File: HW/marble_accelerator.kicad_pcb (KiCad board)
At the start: 2 copper layers, 60 x 60 mm, 23 parts, among them J2 Conn_01x02_Pin, J3 Conn_01x02_Pin, J4 Conn_01x03_Pin, J5 Conn_01x03_Pin, J6 Conn_01x02_Pin, Q1 AO4892, U1 ATmega88P-20A, U2 CNY70, U3 ACS712xLCTR-05B, U4 ACS712xLCTR-05B, U5 L78L05_SO8, U6 EL7202CS

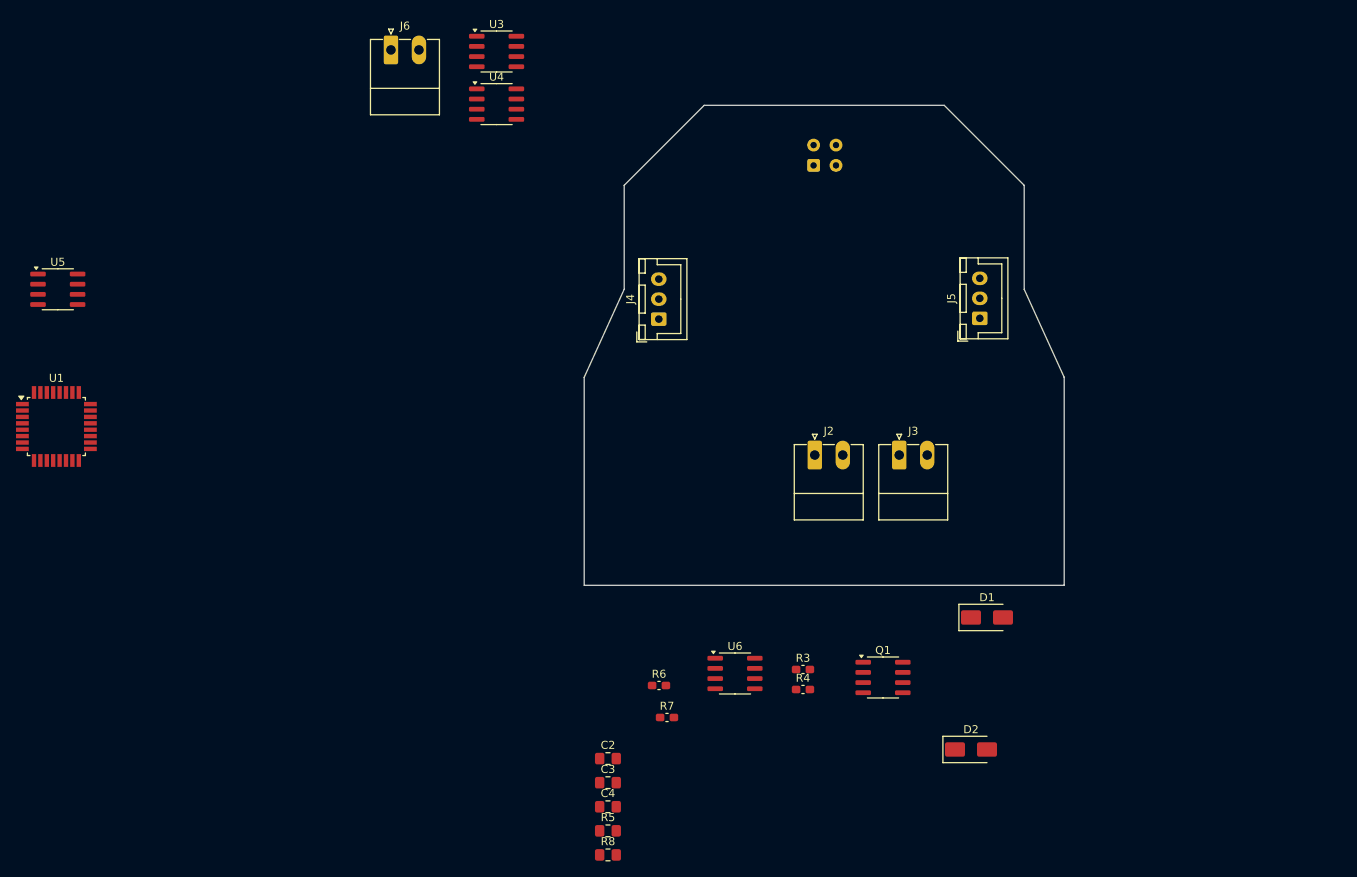
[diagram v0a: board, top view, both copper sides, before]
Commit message: update HW, reduce board to 5x5 cm
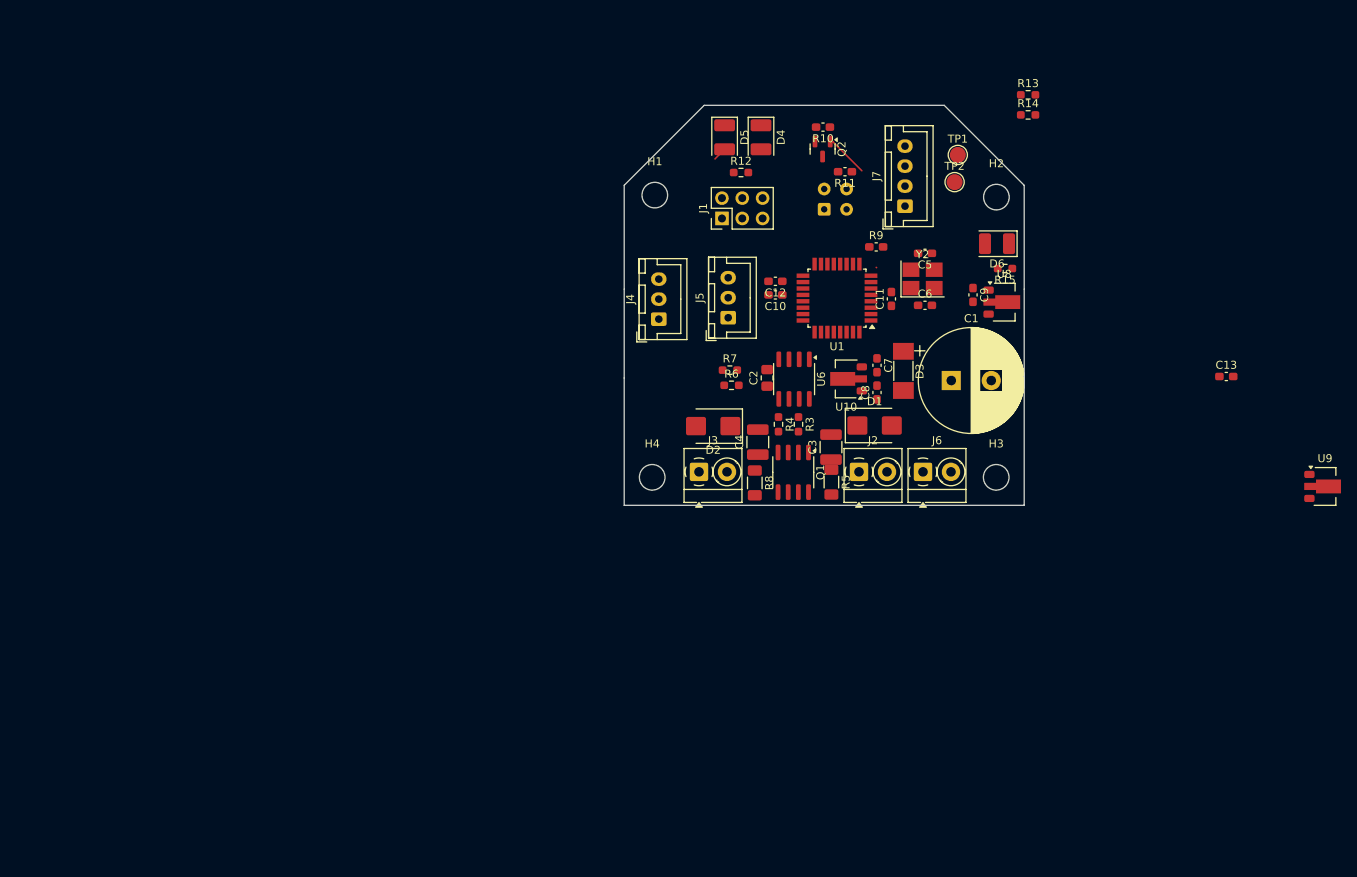
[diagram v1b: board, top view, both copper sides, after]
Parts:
- removed U3, U4: ACS712xLCTR-05B, Package_SO:SOIC-8_3.9x4.9mm_P1.27mm
- removed U5: L78L05_SO8, Package_SO:SOIC-8_3.9x4.9mm_P1.27mm
- added C1: 470µF/50V, Capacitor_THT:CP_Radial_D13.0mm_P5.00mm, F.Cu at (140.9, 74.4)
- added C10: 100nF, Capacitor_SMD:C_0603_1608Metric_Pad1.08x0.95mm_HandSolder, F.Cu at (118.9, 63.7)
- added C11: 100nF, Capacitor_SMD:C_0603_1608Metric_Pad1.08x0.95mm_HandSolder, F.Cu at (133.4, 64.2)
- added C12: 100nF, Capacitor_SMD:C_0603_1608Metric_Pad1.08x0.95mm_HandSolder, F.Cu at (118.9, 62.0)
- added C13: 100nF, Capacitor_SMD:C_0603_1608Metric_Pad1.08x0.95mm_HandSolder, F.Cu at (175.3, 73.9)
- added C5: 22pF, Capacitor_SMD:C_0603_1608Metric_Pad1.08x0.95mm_HandSolder, F.Cu at (137.6, 58.5)
- added C6: 22pF, Capacitor_SMD:C_0603_1608Metric_Pad1.08x0.95mm_HandSolder, F.Cu at (137.6, 65.0)
- added C7: 100nF, Capacitor_SMD:C_0603_1608Metric_Pad1.08x0.95mm_HandSolder, F.Cu at (131.6, 72.5)
- added C8: 100nF, Capacitor_SMD:C_0603_1608Metric_Pad1.08x0.95mm_HandSolder, F.Cu at (131.6, 75.9)
- added C9: 100nF, Capacitor_SMD:C_0603_1608Metric_Pad1.08x0.95mm_HandSolder, F.Cu at (143.6, 63.7)
- added D3: 1N4007, Resistor_SMD:R_MELF_MMB-0207, F.Cu at (134.9, 73.2)
- added D4: LED, LED_SMD:LED_PLCC-2_3.4x3.0mm_KA, F.Cu at (117.1, 44.0)
- added D5: LED, LED_SMD:LED_PLCC-2_3.4x3.0mm_KA, F.Cu at (112.5, 44.0)
- added D6: LED, LED_SMD:LED_PLCC-2_3.4x3.0mm_KA, F.Cu at (146.6, 57.3)
- added H1: MountingHole, MountingHole:MountingHole_3.2mm_M3, F.Cu at (103.8, 51.2)
- added H2: MountingHole, MountingHole:MountingHole_3.2mm_M3, F.Cu at (146.5, 51.5)
- added H3: MountingHole, MountingHole:MountingHole_3.2mm_M3, F.Cu at (146.5, 86.5)
- added H4: MountingHole, MountingHole:MountingHole_3.2mm_M3, F.Cu at (103.5, 86.5)
- added J1: AVR-ISP-6, Connector_PinHeader_2.54mm:PinHeader_2x03_P2.54mm_Vertical, F.Cu at (112.2, 54.1)
- added J7: Conn_01x04_Pin, Connector_JST:JST_XH_B4B-XH-A_1x04_P2.50mm_Vertical, F.Cu at (135.1, 52.6)
- added Q2: BSS138, Package_TO_SOT_SMD:SOT-23, F.Cu at (124.8, 45.5)
- added R10: 10k, Capacitor_SMD:C_0603_1608Metric_Pad1.08x0.95mm_HandSolder, F.Cu at (124.8, 42.7)
- added R11: 150R, Capacitor_SMD:C_0603_1608Metric_Pad1.08x0.95mm_HandSolder, F.Cu at (127.6, 48.3)
- added R12: 10k, Resistor_SMD:R_0603_1608Metric_Pad0.98x0.95mm_HandSolder, F.Cu at (114.6, 48.4)
- added R13: 10k, Resistor_SMD:R_0603_1608Metric_Pad0.98x0.95mm_HandSolder, F.Cu at (150.5, 38.7)
- added R14: 10k, Resistor_SMD:R_0603_1608Metric_Pad0.98x0.95mm_HandSolder, F.Cu at (150.5, 41.2)
- added R15: 10k, Resistor_SMD:R_0603_1608Metric_Pad0.98x0.95mm_HandSolder, F.Cu at (147.6, 60.4)
- added R9: 10k, Capacitor_SMD:C_0603_1608Metric_Pad1.08x0.95mm_HandSolder, F.Cu at (131.5, 57.7)
- added TP1: TestPoint, TestPoint:TestPoint_Pad_D2.0mm, F.Cu at (141.7, 46.2)
- added TP2: TestPoint, TestPoint:TestPoint_Pad_D2.0mm, F.Cu at (141.3, 49.6)
- added U10: L78L12_SOT89, Package_TO_SOT_SMD:SOT-89-3, F.Cu at (127.8, 74.2)
- added U8: L78L05_SOT89, Package_TO_SOT_SMD:SOT-89-3, F.Cu at (147.5, 64.6)
- added U9: MCP1703Ax-500xxMB, Package_TO_SOT_SMD:SOT-89-3, F.Cu at (187.6, 87.6)
- added Y2: Crystal_GND24_Small, Crystal:Crystal_SMD_3225-4Pin_3.2x2.5mm_HandSoldering, F.Cu at (137.3, 61.7)
- C3, C4: footprint Capacitor_SMD:C_0805_2012Metric_Pad1.18x1.45mm_HandSolder -> Capacitor_SMD:C_1210_3225Metric_Pad1.33x2.70mm_HandSolder
- D1, D2: value SMAJ24CA -> SMBJ24CA; footprint Diode_SMD:D_SMA -> Diode_SMD:D_SMB
- J2, J3, J6: footprint Connector_Phoenix_MC:PhoenixContact_MC_1,5_2-G-3.5_1x02_P3.50mm_Horizontal -> TerminalBlock_MetzConnect:TerminalBlock_MetzConnect_Type059_RT06302HBWC_1x02_P3.50mm_Horizontal
- Q1: value AO4892 -> DMTH6016LSD-13
- R3, R4, R6, R7: footprint Capacitor_SMD:C_0603_1608Metric_Pad1.08x0.95mm_HandSolder -> Resistor_SMD:R_0603_1608Metric_Pad0.98x0.95mm_HandSolder
- R5: footprint Capacitor_SMD:C_0805_2012Metric_Pad1.18x1.45mm_HandSolder -> Resistor_SMD:R_1206_3216Metric_Pad1.30x1.75mm_HandSolder
- R8: value 27 -> 47; footprint Capacitor_SMD:C_0805_2012Metric_Pad1.18x1.45mm_HandSolder -> Resistor_SMD:R_1206_3216Metric_Pad1.30x1.75mm_HandSolder
- moved U1 98.9 mm to (126.6, 64.1), turned to 180 degrees
- moved J6 84.9 mm to (137.3, 85.8)
- moved R5 51.8 mm to (125.9, 87.1), turned to -90 degrees
- moved D2 51.7 mm to (111.1, 80.1), turned to 180 degrees
- moved C2 51.6 mm to (117.9, 74.1), turned to 90 degrees
- moved C3 50.4 mm to (125.8, 82.7), turned to 90 degrees
- moved R8 50.0 mm to (116.3, 87.2), turned to -90 degrees
- moved C4 49.3 mm to (116.7, 82.1), turned to 90 degrees
- moved R7 44.1 mm to (113.2, 73.1)
- moved R6 38.6 mm to (113.4, 75.0)
- moved U6 37.5 mm to (121.2, 74.2), turned to -90 degrees
- moved R4 33.3 mm to (119.3, 79.9), turned to -90 degrees
- moved J5 31.5 mm to (113.0, 66.5)
- moved R3 30.7 mm to (121.8, 79.9), turned to -90 degrees
- moved Q1 28.0 mm to (121.1, 85.9), turned to -90 degrees
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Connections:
- J2 pad 1: unconnected-(J2-Pin_1-Pad1) -> /coil driver/COIL0_NEG
- J2 pad 2: unconnected-(J2-Pin_2-Pad2) -> Vdrive
- J3 pad 1: unconnected-(J3-Pin_1-Pad1) -> Vdrive
- J3 pad 2: unconnected-(J3-Pin_2-Pad2) -> /coil driver/COIL1_NEG
- J4 pad 1: unconnected-(J4-Pin_1-Pad1) -> /microcontroller/Hall1
- J4 pad 2: unconnected-(J4-Pin_2-Pad2) -> +5V
- J4 pad 3: unconnected-(J4-Pin_3-Pad3) -> GND
- J5 pad 1: unconnected-(J5-Pin_1-Pad1) -> /microcontroller/Hall0
- J5 pad 2: unconnected-(J5-Pin_2-Pad2) -> +5V
- J5 pad 3: unconnected-(J5-Pin_3-Pad3) -> GND
- J6 pad 1: unconnected-(J6-Pin_1-Pad1) -> Vdrive
- J6 pad 2: unconnected-(J6-Pin_2-Pad2) -> GND
- R6 pad 1: /coil driver/IN_FIRST_COIL -> /coil driver/IN_COIL0
- R7 pad 1: /coil driver/IN_SECOND_COIL -> /coil driver/IN_COIL1
- U1 pad 1: unconnected-(U1-PD3-Pad1) -> Net-(U1-PD3)
- U1 pad 10: unconnected-(U1-PD6-Pad10) -> Net-(D5-A)
- U1 pad 13: unconnected-(U1-PB1-Pad13) -> /microcontroller/EntryEnable
- U1 pad 15: unconnected-(U1-PB3-Pad15) -> /microcontroller/MOSI
- U1 pad 16: unconnected-(U1-PB4-Pad16) -> /microcontroller/MISO
- U1 pad 17: unconnected-(U1-PB5-Pad17) -> /microcontroller/SCK
- U1 pad 18: unconnected-(U1-AVCC-Pad18) -> +5V
- U1 pad 19: unconnected-(U1-ADC6-Pad19) -> /microcontroller/EntrySensor
- U1 pad 2: unconnected-(U1-PD4-Pad2) -> Net-(U1-PD4)
- U1 pad 20: unconnected-(U1-AREF-Pad20) -> Net-(U1-AREF)
- U1 pad 21: Net-(U1-GND-Pad21) -> GND
- U1 pad 23: unconnected-(U1-PC0-Pad23) -> /microcontroller/Hall0
- U1 pad 24: unconnected-(U1-PC1-Pad24) -> /microcontroller/Hall1
- U1 pad 25: unconnected-(U1-PC2-Pad25) -> /coil driver/IN_COIL1
- U1 pad 26: unconnected-(U1-PC3-Pad26) -> /coil driver/IN_COIL0
- U1 pad 29: unconnected-(U1-~{RESET}/PC6-Pad29) -> /microcontroller/!RST
- U1 pad 3: Net-(U1-GND-Pad21) -> GND
- U1 pad 30: unconnected-(U1-PD0-Pad30) -> Net-(J7-Pin_2)
- U1 pad 31: unconnected-(U1-PD1-Pad31) -> Net-(J7-Pin_3)
- U1 pad 4: Net-(U1-VCC-Pad4) -> +5V
- U1 pad 5: Net-(U1-GND-Pad21) -> GND
- U1 pad 6: Net-(U1-VCC-Pad4) -> +5V
- U1 pad 7: unconnected-(U1-XTAL1/PB6-Pad7) -> Net-(U1-XTAL1/PB6)
- U1 pad 8: unconnected-(U1-XTAL2/PB7-Pad8) -> Net-(U1-XTAL2/PB7)
- U1 pad 9: unconnected-(U1-PD5-Pad9) -> Net-(D4-A)
- U2 pad 1: unconnected-(U2-A-Pad1) -> Net-(U2-A)
- U2 pad 2: unconnected-(U2-K-Pad2) -> Net-(Q2-D)
- U2 pad 3: unconnected-(U2-C-Pad3) -> +5V
- U2 pad 4: unconnected-(U2-E-Pad4) -> /microcontroller/EntrySensor
- U6 pad 2: /coil driver/IN_FIRST_COIL -> /coil driver/IN_COIL0
- U6 pad 4: /coil driver/IN_SECOND_COIL -> /coil driver/IN_COIL1
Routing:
- net /microcontroller/EntryEnable: track 0.00 -> 5.47 mm
- net Net-(D5-A): track 0.00 -> 1.77 mm
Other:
- board size 60 x 60 mm -> 50 x 50 mm

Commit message: update HW
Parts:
- added L1: 10µH, Inductor_SMD:L_0603_1608Metric_Pad1.05x0.95mm_HandSolder, F.Cu at (118.9, 60.3)
- added R16: 30k, Resistor_SMD:R_0603_1608Metric_Pad0.98x0.95mm_HandSolder, F.Cu at (104.7, 73.9)
- added R17: 10k, Resistor_SMD:R_0603_1608Metric_Pad0.98x0.95mm_HandSolder, F.Cu at (104.7, 72.1)
- added TP3: TestPoint, TestPoint:TestPoint_Pad_D2.0mm, F.Cu at (137.4, 68.0)
- moved R14 42.3 mm to (108.5, 46.0), turned to 90 degrees
- moved C13 32.7 mm to (143.6, 65.7), turned to 90 degrees
- moved R13 31.3 mm to (120.3, 46.9), turned to 90 degrees
- moved R6 8.93 mm to (119.2, 68.2), turned to 180 degrees
- moved R7 6.84 mm to (119.2, 69.8), turned to 180 degrees
- moved R11 6.64 mm to (121.9, 51.7), turned to -90 degrees
- moved D5 4.45 mm to (117.0, 43.9), turned to 90 degrees
- moved D4 4.10 mm to (113.0, 43.8), turned to 90 degrees
- moved C9 1.30 mm to (143.6, 62.4)
- moved U8 0.80 mm to (147.5, 63.8)
- moved R15 0.70 mm to (147.6, 59.7)
- moved C3 0.63 mm to (125.5, 82.2)
- moved R5 0.41 mm to (125.5, 87.2)
- moved R8 0.38 mm to (116.7, 87.2)
- moved H1 0.37 mm to (103.5, 51.4)
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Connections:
- C12 pad 1: +5V -> Net-(U1-AVCC)
- U1 pad 18: +5V -> Net-(U1-AVCC)
- U1 pad 22: unconnected-(U1-ADC7-Pad22) -> Net-(U1-ADC7)
- U1 pad 27: unconnected-(U1-PC4-Pad27) -> Net-(U1-PC4)
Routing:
- net Vdrive: track 0.00 -> 54.7 mm
- net Net-(J7-Pin_3): track 0.00 -> 38.0 mm
- net Net-(D4-A): track 0.00 -> 36.8 mm
- net Net-(J7-Pin_2): track 0.00 -> 35.9 mm
- net Net-(D5-A): track 1.77 -> 31.9 mm
- net Net-(U1-ADC7): track 0.00 -> 27.6 mm
- net /microcontroller/Hall1: track 0.00 -> 18.8 mm
- net /microcontroller/EntryEnable: track 5.47 -> 22.8 mm
- net /coil driver/COIL1_NEG: track 0.00 -> 15.1 mm
- net /microcontroller/MISO: track 0.00 -> 14.9 mm
- net /coil driver/COIL0_NEG: track 0.00 -> 14.8 mm
- net Net-(U1-PC4): track 0.00 -> 14.7 mm
- net +12V: track 0.00 -> 14.6 mm
- net GND: track 0.00 -> 13.9 mm
- net Net-(D3-K): track 0.00 -> 13.8 mm
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
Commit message: update layout
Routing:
- net /microcontroller/SCK: track 0.00 -> 28.1 mm
- net Net-(D4-K): track 0.00 -> 4.59 mm
- net +5V: track 8.98 -> 13.1 mm
- net /microcontroller/MOSI: track 13.4 -> 17.3 mm
- net Net-(D5-K): track 0.00 -> 3.54 mm
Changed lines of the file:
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@@
+	)
+	(segment
+		(start 113.6875 48.4)
+		(end 113.1 48.4)
+		(width 0.2)
+		(layer "F.Cu")
+		(net 18)
+	)
+	(segment
+		(start 112.22 49.28)
+		(end 112.22 51.6)
+		(width 0.2)
+		(layer "F.Cu")
+		(net 18)
+	)
+	(segment
+		(start 113.1 48.4)
+		(end 112.22 49.28)
+		(width 0.2)
+		(layer "F.Cu")
+		(net 18)
 	)
 	(segment
@@
 	)
 	(segment
+		(start 112.5 52.989)
+		(end 112.5 52.94776)
+		(width 0.2)
+		(layer "F.Cu")
+		(net 23)
+	)
+	(segment
+		(start 121.3 61.3)
+		(end 121 61)
+		(width 0.2)
+		(layer "F.Cu")
+		(net 23)
+	)
+	(segment
+		(start 115.449 50.449)
+		(end 115.911 50.911)
+		(width 0.2)
+		(layer "F.Cu")
+		(net 23)
+	)
+	(segment
+		(start 114.051 50.449)
+		(end 115.449 50.449)
+		(width 0.2)
+		(layer "F.Cu")
+		(net 23)
+	)
+	(segment
+		(start 110.5 54.722)
+		(end 110.5 53.5)
+		(width 0.2)
+		(layer "F.Cu")
+		(net 23)
+	)
+	(segment
+		(start 121 59)
+		(end 119.5 57.5)
+		(width 0.2)
+		(layer "F.Cu")
+		(net 23)
+	)
+	(segment
+		(start 119.5 57.5)
+		(end 113.278 57.5)
+		(width 0.2)
+		(layer "F.Cu")
+		(net 23)
+	)
+	(segment
+		(start 121 61)
+		(end 121 59)
+		(width 0.2)
+		(layer "F.Cu")
+		(net 23)
+	)
+	(segment
+		(start 112.5 52.94776)
+		(end 113.371 52.07676)
+		(width 0.2)
+		(layer "F.Cu")
+		(net 23)
+	)
+	(segment
+		(start 110.5 53.5)
+		(end 111.011 52.989)
+		(width 0.2)
+		(layer "F.Cu")
+		(net 23)
+	)
+	(segment
+		(start 115.911 52.989)
+		(end 114.76 54.14)
+		(width 0.2)
+		(layer "F.Cu")
+		(net 23)
+	)
+	(segment
+		(start 113.371 52.07676)
+		(end 113.371 51.129)
+		(width 0.2)
+		(layer "F.Cu")
+		(net 23)
+	)
+	(segment
+		(start 111.011 52.989)
+		(end 112.5 52.989)
+		(width 0.2)
+		(layer "F.Cu")
+		(net 23)
+	)
+	(segment
+		(start 122.35 61.3)
+		(end 121.3 61.3)
+		(width 0.2)
+		(layer "F.Cu")
+		(net 23)
+	)
+	(segment
+		(start 115.911 50.911)
+		(end 115.911 52.989)
+		(width 0.2)
+		(layer "F.Cu")
+		(net 23)
+	)
+	(segment
+		(start 113.278 57.5)
+		(end 110.5 54.722)
+		(width 0.2)
+		(layer "F.Cu")
+		(net 23)
+	)
+	(segment
+		(start 113.371 51.129)
+		(end 114.051 50.449)
+		(width 0.2)
+		(layer "F.Cu")
+		(net 23)
+	)
+	(segment
 		(start 115.199 56.599)
 		(end 113.609 55.009)
@@
 		(start 124.6 59.1)
 		(end 122.099 56.599)
+		(width 0.2)
+		(layer "F.Cu")
+		(net 25)
+	)
+	(segment
+		(start 113.609 52.751)
+		(end 113.609 55.009)
+		(width 0.2)
+		(layer "F.Cu")
+		(net 25)
+	)
+	(segment
+		(start 114.76 51.6)
+		(end 113.609 52.751)
 		(width 0.2)
 		(layer "F.Cu")
@@
 	)
 	(segment
+		(start 108.7125 45.3)
+		(end 108.5 45.0875)
+		(width 0.2)
+		(layer "F.Cu")
+		(net 38)
+	)
+	(segment
+		(start 113 45.3)
+		(end 108.7125 45.3)
+		(width 0.2)
+		(layer "F.Cu")
+		(net 38)
+	)
+	(segment
 		(start 130.6 42.7)
 		(end 128.5 40.6)
@@
 	)
 	(segment
+		(start 117 45.4)
+		(end 119.7125 45.4)
+		(width 0.2)
+		(layer "F.Cu")
+		(net 41)
+	)
+	(segment
+		(start 119.7125 45.4)
+		(end 120.3 45.9875)
+		(width 0.2)
+		(layer "F.Cu")
+		(net 41)
+	)
+	(segment

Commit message: update layout
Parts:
- added C14: 100nF, Capacitor_SMD:C_0603_1608Metric_Pad1.08x0.95mm_HandSolder, F.Cu at (104.6, 70.5)
- moved TP3 0.10 mm to (137.5, 68.0)
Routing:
- net /microcontroller/!RST: track 0.00 -> 36.3 mm, vias 0 -> 3
- net +12V: track 14.6 -> 42.1 mm
- net Vdrive: track 54.7 -> 63.7 mm
- net Net-(U1-ADC7): track 27.6 -> 31.0 mm
- net Net-(J7-Pin_2): track 35.9 -> 35.1 mm

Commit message: update layout and schematic
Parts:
- removed U9: MCP1703Ax-500xxMB, Package_TO_SOT_SMD:SOT-89-3
- added R18: 0R, Resistor_SMD:R_0603_1608Metric_Pad0.98x0.95mm_HandSolder, F.Cu at (132.1, 74.4)
- C14: value 100nF -> 100µF/25V; footprint Capacitor_SMD:C_0603_1608Metric_Pad1.08x0.95mm_HandSolder -> Capacitor_THT:CP_Radial_D6.3mm_P2.50mm
- moved R15 48.7 mm to (102.6, 78.3)
- moved D6 46.6 mm to (102.9, 73.3), turned to 90 degrees
- moved C14 38.8 mm to (141.0, 57.0)
- moved R9 11.3 mm to (128.0, 47.0), turned to 90 degrees
- moved R6 7.29 mm to (125.8, 71.3), turned to 0 degrees
- moved R17 4.66 mm to (109.2, 73.3), turned to 180 degrees
- moved R16 4.63 mm to (109.2, 75.0), turned to 0 degrees
- moved J5 2.07 mm to (111.0, 66.0)
- moved C11 1.20 mm to (132.2, 64.2)
- moved Y2 1.20 mm to (136.1, 61.7)
- moved C10 1.20 mm to (117.7, 63.7)
- moved C12 1.20 mm to (117.7, 62.0)
- moved L1 1.20 mm to (117.7, 60.3)
- moved C6 1.20 mm to (136.4, 65.0)
- moved U1 1.20 mm to (125.4, 64.1)
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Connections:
- C14 pad 1: Net-(U1-ADC7) -> +5V
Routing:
- net /microcontroller/!RST: track 36.3 -> 0.00 mm, vias 3 -> 0
- net +12V: track 42.1 -> 9.66 mm
- net Net-(U1-ADC7): track 31.0 -> 0.00 mm
- net /microcontroller/EntrySensor: track 0.00 -> 20.9 mm, vias 0 -> 4
- net +5V: track 13.1 -> 22.8 mm
- net /microcontroller/SCK: track 28.1 -> 20.1 mm
- net Net-(D4-K): track 4.59 -> 0.00 mm
- net /coil driver/COIL0_NEG: track 14.8 -> 19.1 mm
- net Net-(D3-K): track 13.8 -> 9.91 mm
- net GND: track 13.9 -> 10.3 mm, vias 0 -> 10
- net Net-(D5-K): track 3.54 -> 0.00 mm
- net /microcontroller/MOSI: track 17.5 -> 15.5 mm
- net /coil driver/IN_COIL0: track 9.31 -> 7.32 mm, vias 2 -> 0
- net Net-(J7-Pin_3): track 38.4 -> 36.6 mm
- net Net-(U1-AVCC): track 4.33 -> 2.65 mm
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- added copper zone on F.Cu, net /coil driver/COIL0_NEG
- added copper zone on F.Cu, net /coil driver/COIL1_NEG
- added copper zone on B.Cu, net GND
- added copper zone on F.Cu, net GND

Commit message: update schematic and board
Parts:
- moved TP3 14.5 mm to (147.8, 57.8)
- moved TP2 12.6 mm to (131.3, 57.2)
- moved R7 1.10 mm to (118.1, 69.7)
- moved D3 0.73 mm to (135.1, 73.9)
- moved R15 0.28 mm to (102.8, 78.1), turned to 0 degrees
- moved R4 0.08 mm to (119.2, 79.9)
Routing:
- net /microcontroller/!RST: track 0.00 -> 41.8 mm, vias 0 -> 5
- net Net-(U1-PD3): track 0.00 -> 40.9 mm
- net Net-(U1-ADC7): track 0.00 -> 36.9 mm
- net Net-(U1-PD4): track 0.00 -> 25.7 mm
- net Net-(U1-PC4): track 15.6 -> 37.6 mm
- net Net-(D3-K): track 9.91 -> 0.00 mm
- net +12V: track 9.66 -> 17.1 mm
- net Vdrive: track 64.7 -> 69.9 mm
- net +5V: track 22.8 -> 27.9 mm
- net Net-(J7-Pin_2): track 34.3 -> 38.2 mm
- net /coil driver/IN_COIL0: track 7.32 -> 4.44 mm
- net Net-(J7-Pin_3): track 36.6 -> 38.3 mm
- net /coil driver/IN_COIL1: track 5.68 -> 7.00 mm
- net GND: track 10.3 -> 10.8 mm, vias 10 -> 14

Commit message: finished first layout
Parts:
- added C6: 100nF, Capacitor_SMD:C_0603_1608Metric_Pad1.08x0.95mm_HandSolder, F.Cu at (109.2, 71.5)
- added R4: 1k, Capacitor_SMD:C_0603_1608Metric_Pad1.08x0.95mm_HandSolder, F.Cu at (117.7, 65.4)
- added R5: 1k, Capacitor_SMD:C_0603_1608Metric_Pad1.08x0.95mm_HandSolder, F.Cu at (117.7, 66.9)
- moved TP1 38.3 mm to (113.1, 74.0)
- moved R2 11.0 mm to (120.2, 54.7)
- moved R10 9.90 mm to (109.7, 57.0)
- moved R17 7.23 mm to (124.9, 75.1), turned to 90 degrees
- moved C14 6.16 mm to (126.4, 77.0), turned to 90 degrees
- moved C13 4.70 mm to (126.4, 73.7), turned to -90 degrees
- moved U4 3.01 mm to (130.0, 74.8), turned to 0 degrees
- moved C4 1.84 mm to (135.5, 56.9), turned to 0 degrees
- moved D6 1.60 mm to (102.9, 74.9)
- moved Y1 1.26 mm to (135.7, 60.5), turned to 90 degrees
- moved C5 0.89 mm to (136.0, 64.2), turned to 180 degrees
- moved D1 0.70 mm to (113.0, 44.5)
- moved D2 0.63 mm to (116.8, 44.5)
- moved R8 0.54 mm to (120.1, 46.4)
- moved TP2 0.45 mm to (141.3, 46.4)
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- renumbered C11 to C1, C9 to C10, C14 to C11, C13 to C12, C8 to C13, C7 to C14, C1 to C15, C12 to C2, C10 to C3, C5 to C4, C6 to C5, C2 to C7, C3 to C8, C4 to C9, D4 to D1, D5 to D2, D1 to D3, D2 to D4, D3 to D5, H2 to H1, H1 to H2, H4 to H3, H3 to H4, J6 to J1, J5 to J3, J3 to J4, J4 to J5, J7 to J6, J1 to J7, Q2 to Q1, Q1 to Q2, R11 to R1, R12 to R10, R5 to R11, R3 to R12, R6 to R13, R7 to R14, R4 to R15, R8 to R16, R18 to R17, R15 to R18, R9 to R2, R10 to R3, R16 to R6, R17 to R7, R13 to R8, R14 to R9, TP3 to TP1, TP1 to TP2, TP2 to TP3, U2 to U1, U1 to U2, U6 to U3, U10 to U4, U8 to U5, Y2 to Y1
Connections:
- D1 pad 2: Net-(D4-A) -> Net-(D1-A)
- D2 pad 2: Net-(D5-A) -> Net-(D2-A)
- J3 pad 1: /microcontroller/Hall0 -> Net-(J3-Pin_1)
- J5 pad 1: /microcontroller/Hall1 -> Net-(J5-Pin_1)
- R6 pad 2: Net-(U1-ADC7) -> Net-(U2-ADC6)
- R7 pad 1: Net-(U1-ADC7) -> Net-(U2-ADC6)
- U2 pad 10: Net-(D5-A) -> Net-(D1-A)
- U2 pad 11: unconnected-(U1-PD7-Pad11) -> Net-(D2-A)
- U2 pad 13: /microcontroller/EntryEnable -> unconnected-(U2-PB1-Pad13)
- U2 pad 19: /microcontroller/EntrySensor -> Net-(U2-ADC6)
- U2 pad 22: Net-(U1-ADC7) -> /microcontroller/Hall0
- U2 pad 23: /microcontroller/Hall0 -> /microcontroller/Hall1
- U2 pad 24: /microcontroller/Hall1 -> /microcontroller/EntrySensor
- U2 pad 9: Net-(D4-A) -> /microcontroller/EntryEnable
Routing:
- net +5V: track 27.9 -> 120.8 mm, vias 0 -> 4
- net Net-(D4-A): track 37.3 -> 0.00 mm
- net Net-(U1-ADC7): track 36.9 -> 0.00 mm
- net GND: track 10.8 -> 47.7 mm, vias 14 -> 70
- net Net-(D1-A): track 0.00 -> 36.9 mm, vias 0 -> 2
- net Net-(U2-ADC6): track 0.00 -> 35.9 mm
- net Net-(D5-A): track 32.4 -> 0.00 mm
- net Net-(D2-A): track 0.00 -> 27.5 mm
- net Net-(D5-K): track 0.00 -> 27.1 mm
- net Net-(U2-PC4): track 37.6 -> 17.1 mm, vias 0 -> 2
- net +12V: track 17.1 -> 37.5 mm
- net /microcontroller/Hall1: track 17.1 -> 3.09 mm
- net Net-(J5-Pin_1): track 0.00 -> 12.8 mm
- net /coil driver/COIL0_NEG: track 19.1 -> 6.79 mm
- net /microcontroller/EntrySensor: track 20.9 -> 32.7 mm
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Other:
- board text added: "+"
- board text added: "-"
- board text added: "1"
- board text added: "5V"
- board text added: "COIL1"
- board text added: "GND"
- board text added: "HALL0"
- board text added: "HALL1"
- board text added: "PWR"
- board text added: "RX"
- board text added: "TX"

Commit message: first HW order state
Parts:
- J6: value Conn_01x04_Pin -> UART; footprint Connector_JST:JST_XH_B4B-XH-A_1x04_P2.50mm_Vertical -> Connector_PinHeader_2.54mm:PinHeader_1x04_P2.54mm_Vertical
- moved Q1 0.15 mm to (125.0, 45.5)
- moved R3 0.15 mm to (125.0, 42.7)
- moved J6 0.14 mm to (135.0, 52.7), turned to 180 degrees
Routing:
- net Net-(U2-PD3): track 40.6 -> 42.5 mm
- net Net-(J6-Pin_3): track 37.9 -> 38.8 mm
